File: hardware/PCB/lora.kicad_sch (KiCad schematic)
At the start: 8 parts, among them J2 LoRa_prog, U7 WLR089U0-I_RM

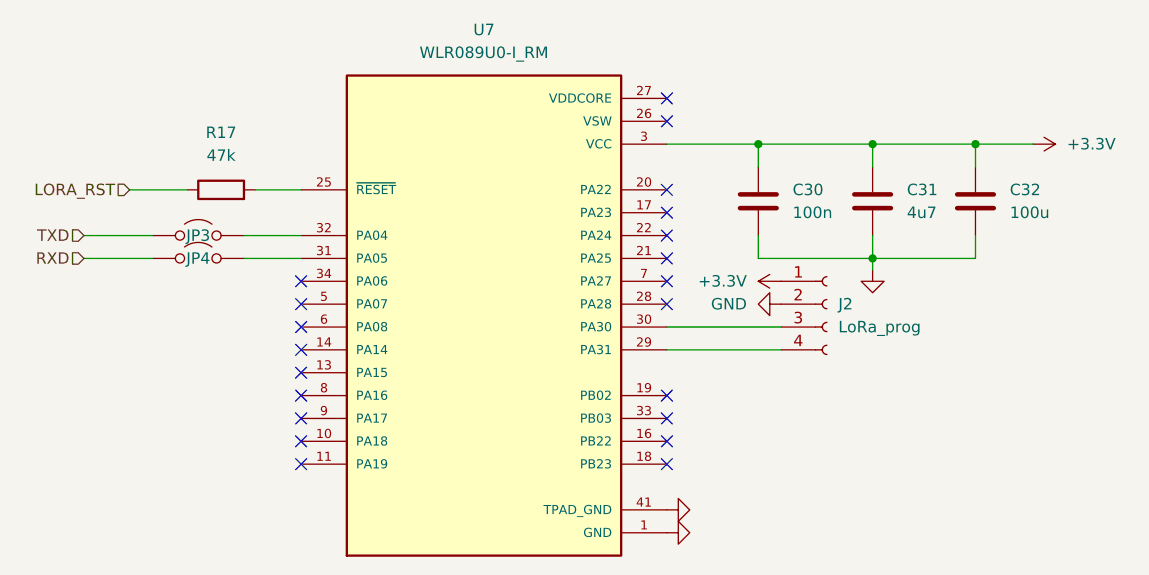
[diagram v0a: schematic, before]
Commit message: Changed LoRa modul on PCB
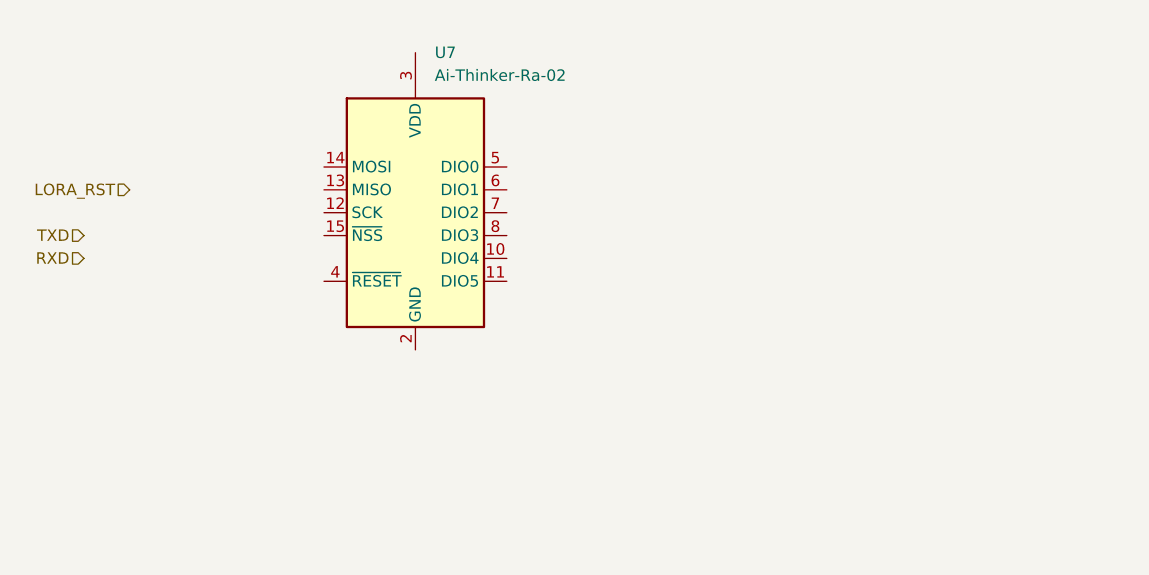
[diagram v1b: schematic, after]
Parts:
- removed C30: 100n, Capacitor_SMD:C_1206_3216Metric_Pad1.33x1.80mm_HandSolder, symbol Device:C
- removed C31: 4u7, Capacitor_SMD:C_1206_3216Metric_Pad1.33x1.80mm_HandSolder, symbol Device:C
- removed C32: 100u, Capacitor_SMD:C_1206_3216Metric_Pad1.33x1.80mm_HandSolder, symbol Device:C
- removed J2: LoRa_prog, Connector_PinSocket_2.54mm:PinSocket_1x04_P2.54mm_Vertical, symbol Connector:Conn_01x04_Socket
- removed JP3, JP4: Jumper_2_Open, Jumper:SolderJumper-2_P1.3mm_Open_RoundedPad1.0x1.5mm, symbol Jumper:Jumper_2_Open
- removed R17: 47k, Resistor_SMD:R_1206_3216Metric_Pad1.30x1.75mm_HandSolder, symbol Device:R
- removed U7: WLR089U0-I_RM, WLR089U0-I_RM:MODULE_WLR089U0-I_RM, symbol WLR089U0-I_RM:WLR089U0-I_RM
- added U7: Ai-Thinker-Ra-02, RF_Module:Ai-Thinker-Ra-01-LoRa, symbol RF_Module:Ai-Thinker-Ra-02
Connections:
- new net: U7.1 (GND), U7.16 (GND), U7.2 (GND), U7.9 (GND)
- no-connect marks 21 -> 0

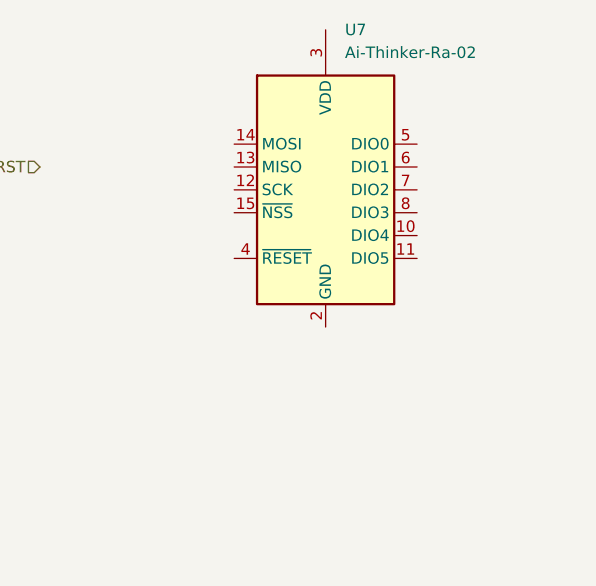
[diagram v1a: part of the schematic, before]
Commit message: Added I2C expander for motor drivers and changed LoRa module
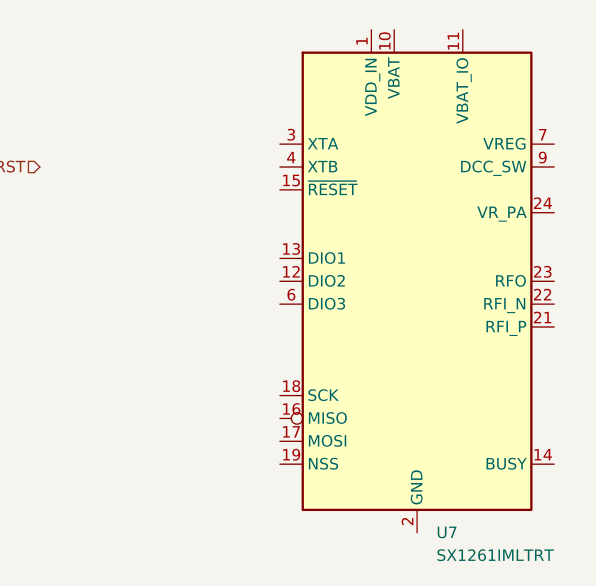
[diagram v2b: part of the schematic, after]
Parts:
- removed U7: Ai-Thinker-Ra-02, RF_Module:Ai-Thinker-Ra-01-LoRa, symbol RF_Module:Ai-Thinker-Ra-02
- added U7: SX1261IMLTRT, Package_DFN_QFN:QFN-24-1EP_4x4mm_P0.5mm_EP2.15x2.15mm, symbol RF:SX1261IMLTRT
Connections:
- new net: U7.2 (GND), U7.20 (GND), U7.25 (GND), U7.5 (GND), U7.8 (GND)
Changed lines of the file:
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@@
 	)
 	(symbol
-		(lib_id "RF_Module:Ai-Thinker-Ra-02")
-		(at 127 69.85 0)
+		(lib_id "RF:SX1261IMLTRT")
+		(at 137.16 80.01 0)
 		(unit 1)
 		(exclude_from_sim no)
@@
 		(fields_autoplaced yes)
 		(property "Reference" "U7"
-			(at 129.1433 52.07 0)
+			(at 139.3033 107.95 0)
 			(effects
 				(font
@@
 			)
 		)
-		(property "Value" "Ai-Thinker-Ra-02"
-			(at 129.1433 54.61 0)
+		(property "Value" "SX1261IMLTRT"
+			(at 139.3033 110.49 0)
 			(effects
 				(font
@@
 			)
 		)
-		(property "Footprint" "RF_Module:Ai-Thinker-Ra-01-LoRa"
-			(at 152.4 80.01 0)
+		(property "Footprint" "Package_DFN_QFN:QFN-24-1EP_4x4mm_P0.5mm_EP2.15x2.15mm"
+			(at 138.43 111.76 0)
 			(effects
 				(font
@@
 			)
 		)
-		(property "Datasheet" "http://wiki.ai-thinker.com/_media/lora/docs/c048ps01a1_ra-02_product_specification_v1.1.pdf"
-			(at 129.54 50.8 0)
+		(property "Datasheet" "https://semtech.file.force.com/sfc/dist/version/download/?oid=00DE0000000JelG&ids=0682R00000IjPWSQA3&d=%2Fa%2F2R000000Un7F%2FyT.fKdAr9ZAo3cJLc4F2cBdUsMftpT2vsOICP7NmvMo"
+			(at 138.43 109.22 0)
 			(effects
 				(font
@@
 			)
 		)
-		(property "Description" "Ai-Thinker Ra-02 410-525 MHz LoRa Module, SPI interface, U.FL antenna connector"
-			(at 127 69.85 0)
+		(property "Description" "150 MHz to 960 MHz Low Power Long Range Transceiver, 14dBm output power, spreading factor from 5 to 12, LoRA, QFN-24"
+			(at 137.16 80.01 0)
 			(effects
 				(font
@@
 			)
 		)
-		(pin "11"
+		(pin "20"
+		)
+		(pin "2"
+		)
+		(pin "14"
 		)
 		(pin "10"
 		)
-		(pin "14"
+		(pin "9"
+		)
+		(pin "18"
+		)
+		(pin "21"
+		)
+		(pin "24"
+		)
+		(pin "6"
 		)
 		(pin "13"
 		)
-		(pin "12"
-		)
 		(pin "15"
-		)
-		(pin "2"
 		)
 		(pin "4"
@@
 		(pin "3"
 		)
-		(pin "1"
+		(pin "8"
+		)
+		(pin "25"
+		)
+		(pin "11"
+		)
+		(pin "22"
+		)
+		(pin "23"
+		)
+		(pin "19"
+		)
+		(pin "5"
 		)
 		(pin "7"
 		)
-		(pin "8"
+		(pin "1"
 		)
-		(pin "6"
-		)
-		(pin "5"
-		)
-		(pin "9"
+		(pin "12"
 		)
 		(pin "16"
 		)
+		(pin "17"
+		)
 		(instances

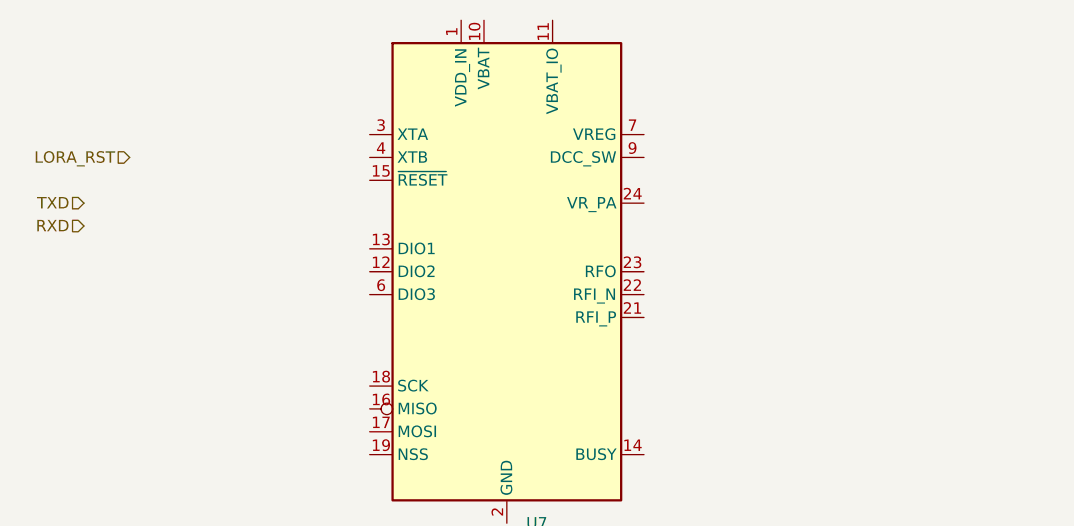
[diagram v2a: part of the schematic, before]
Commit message: Started RF design for LoRa chip
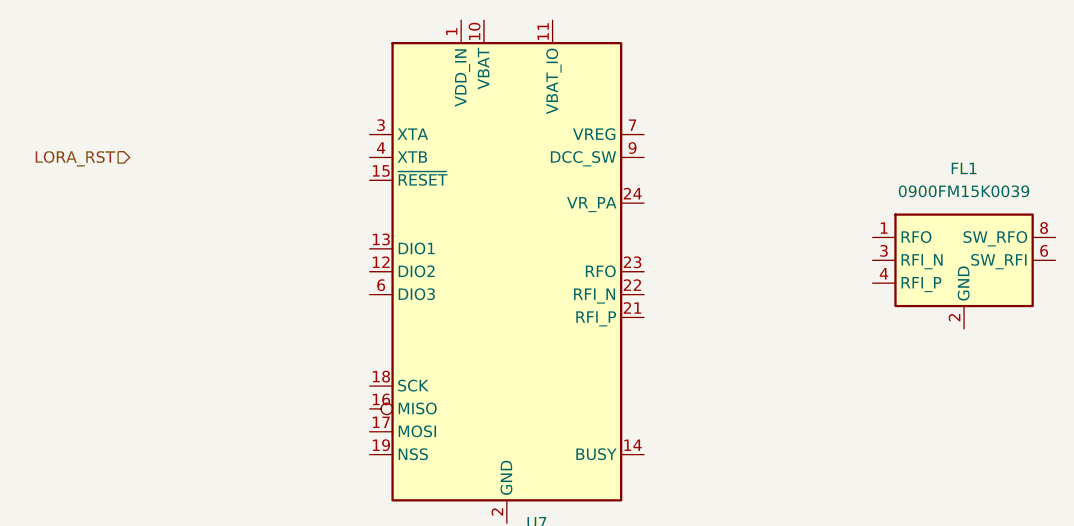
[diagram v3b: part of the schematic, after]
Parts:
- added FL1: 0900FM15K0039, RF_Converter:Balun_Johanson_0900FM15K0039, symbol Filter:0900FM15K0039
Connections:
- new net: FL1.10 (GND), FL1.2 (GND), FL1.5 (GND), FL1.7 (GND), FL1.9 (GND)
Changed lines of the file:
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@@
-		)
-	)
-	(hierarchical_label "TXD"
-		(shape input)
-		(at 90.17 72.39 180)
-		(effects
-			(font
-				(size 1.27 1.27)
-			)
-			(justify right)
-		)
-	)
-	(hierarchical_label "RXD"
-		(shape input)
-		(at 90.17 74.93 180)
-		(effects
-			(font
-				(size 1.27 1.27)
-			)
-			(justify right)
 		)
 	)
@@
 					(unit 1)
 				)
+			)
+		)
+	)
+	(symbol
+		(lib_id "Filter:0900FM15K0039")
+		(at 187.96 78.74 0)
+		(unit 1)
+		(exclude_from_sim no)
+		(in_bom yes)
+		(on_board yes)
+		(dnp no)
+		(fields_autoplaced yes)
+		(property "Reference" "FL1"
+			(at 187.96 68.58 0)
+			(effects
+				(font
+					(size 1.27 1.27)
+				)
+			)
+		)
+		(property "Value" "0900FM15K0039"
+			(at 187.96 71.12 0)
+			(effects
+				(font
+					(size 1.27 1.27)
+				)
+			)
+		)
+		(property "Footprint" "RF_Converter:Balun_Johanson_0900FM15K0039"
+			(at 187.96 88.265 0)
+			(effects
+				(font
+					(size 1.27 1.27)
+				)
+				(hide yes)
+			)
+		)
+		(property "Datasheet" "https://www.johansontechnology.com/datasheets/0900FM15K0039/0900FM15K0039.pdf"
+			(at 188.595 90.17 0)
+			(effects
+				(font
+					(size 1.27 1.27)
+				)
+				(hide yes)
+			)
+		)
+		(property "Description" "868MHz/915MHz Sub-GHz Impedance Matched Filter integrated passive for Semtech SX1261, SX1262, LLCC68"
+			(at 187.96 78.74 0)
+			(effects
+				(font
+					(size 1.27 1.27)
+				)
+				(hide yes)
+			)
+		)
+		(pin "6"
+		)
+		(pin "10"
+		)
+		(pin "9"
+		)
+		(pin "1"
+		)
+		(pin "8"
+		)
+		(pin "2"
+		)
+		(pin "4"
+		)
+		(pin "3"
+		)
+		(pin "7"
+		)
+		(pin "5"
+		)
+		(instances
+			(project ""
+				(path "/45ea479c-a8ef-4c14-88b0-391ede4fd156/efc52d26-5e7f-40f5-a09a-58b8b5321559"
+					(reference "FL1")
+					(unit 1)
+				)

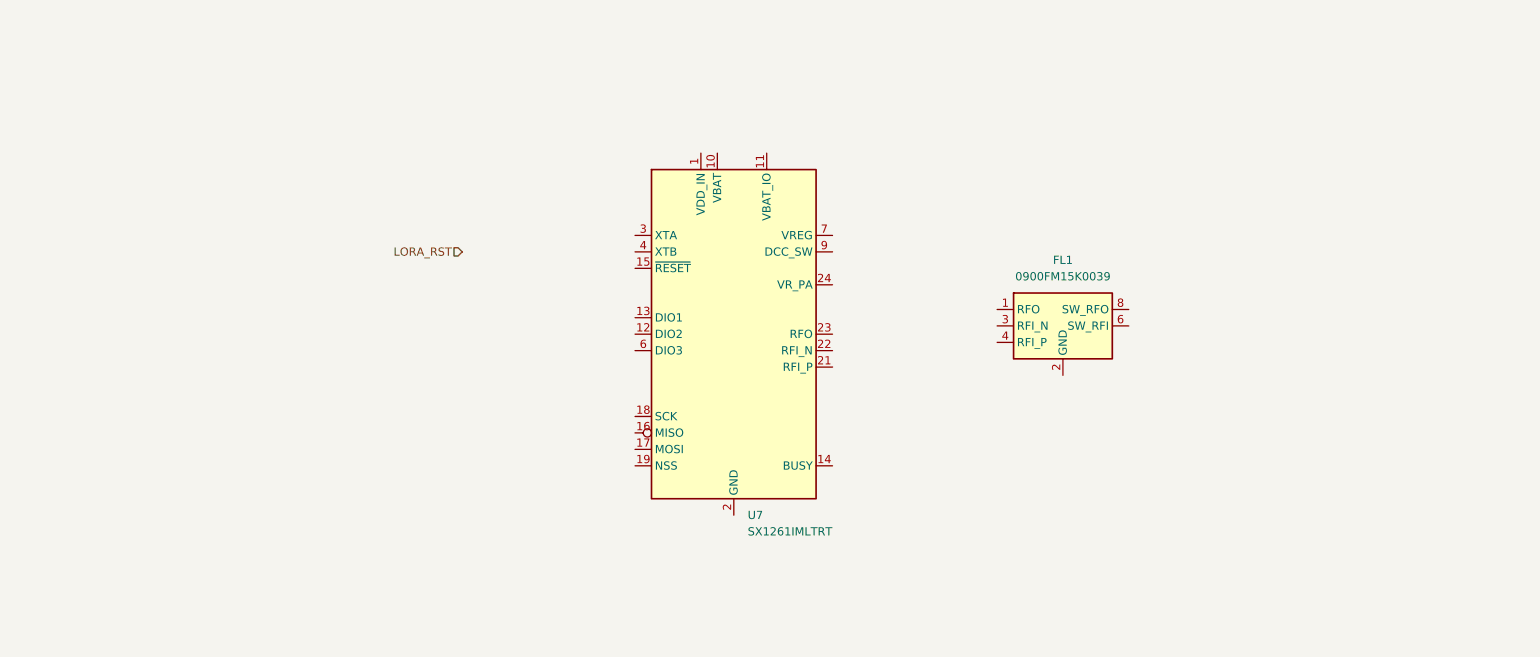
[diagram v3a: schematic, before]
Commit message: Started shcematic design for LoRa chip
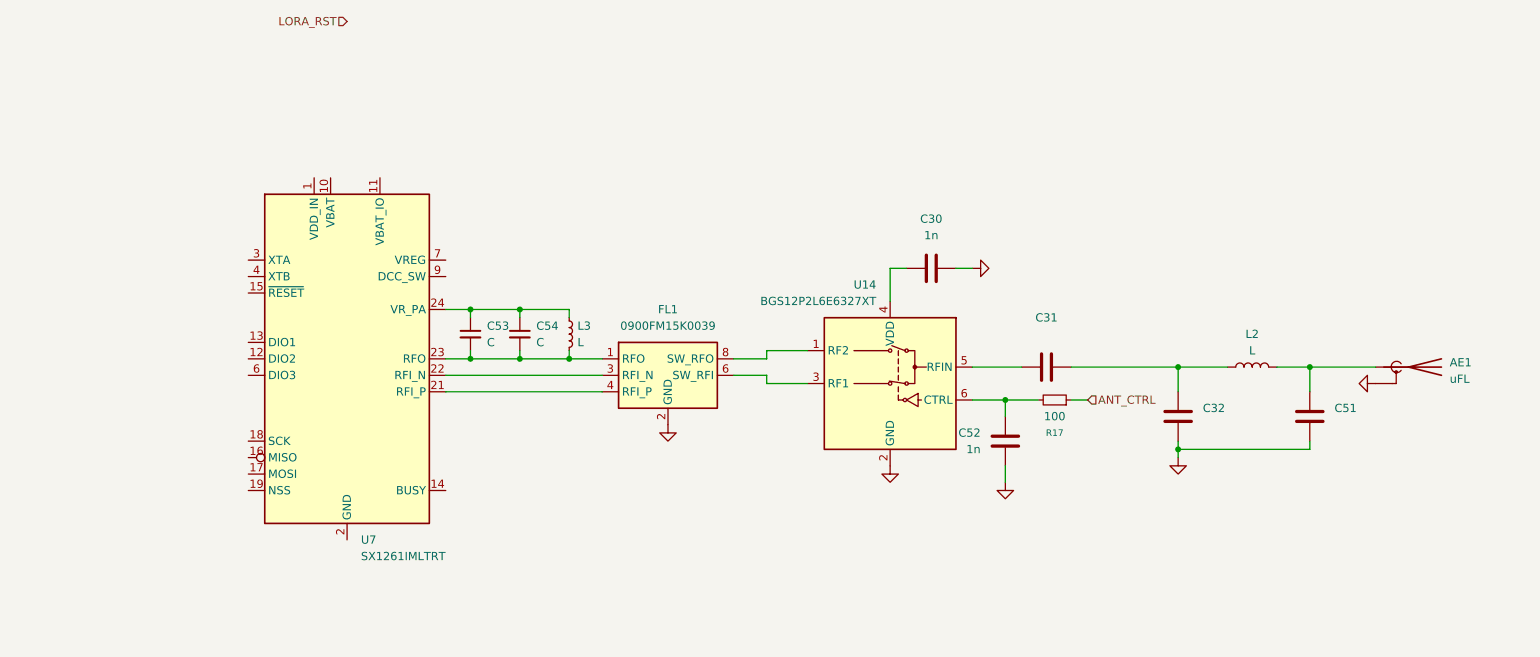
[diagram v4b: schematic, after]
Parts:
- added AE1: uFL, symbol Device:Antenna_Shield
- added C30, C52: 1n, symbol Device:C
- added C31, C32, C51: ~, symbol Device:C
- added C53, C54: C, symbol Device:C_Small
- added L2: L, symbol Device:L
- added L3: L, symbol Device:L_Small
- added R17: 100, symbol Device:R_Small
- added U14: BGS12P2L6E6327XT, Package_LGA:Infineon_PG-TSNP-6-10_0.7x1.1mm_0.7x1.1mm_P0.4mm, symbol RF_Switch:BGS12WN6E6327
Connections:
- net at U7.21 (RFI_P): now also FL1.4 (RFI_P)
- net at U7.22 (RFI_N): now also FL1.3 (RFI_N)
- net at U7.23 (RFO): now also FL1.1 (RFO), C53.2, C54.2, L3.2
- net at U7.24 (VR_PA): now also C53.1, C54.1, L3.1
- net GND: now reaches FL1.10 (GND), FL1.2 (GND), FL1.5 (GND), FL1.7 (GND), FL1.9 (GND)
- net GND: now also AE1.2 (Shield), C30.2, C32.1, C51.1, C52.1, U14.2 (GND)
- net at FL1.6 (SW_RFI): now also U14.3 (RF1)
- net at FL1.8 (SW_RFO): now also U14.1 (RF2)
- new net: C30.1, U14.4 (VDD)
- new net: C52.2, R17.2, U14.6 (CTRL)
- new net: C31.2, C32.2, L2.1
- new net: C31.1, U14.5 (RFIN)
- new net: AE1.1 (A), C51.2, L2.2
- new net ANT_CTRL: R17.1
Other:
- moved on the sheet: FL1, U7

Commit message: Finished schematic for LoRa, added BME280
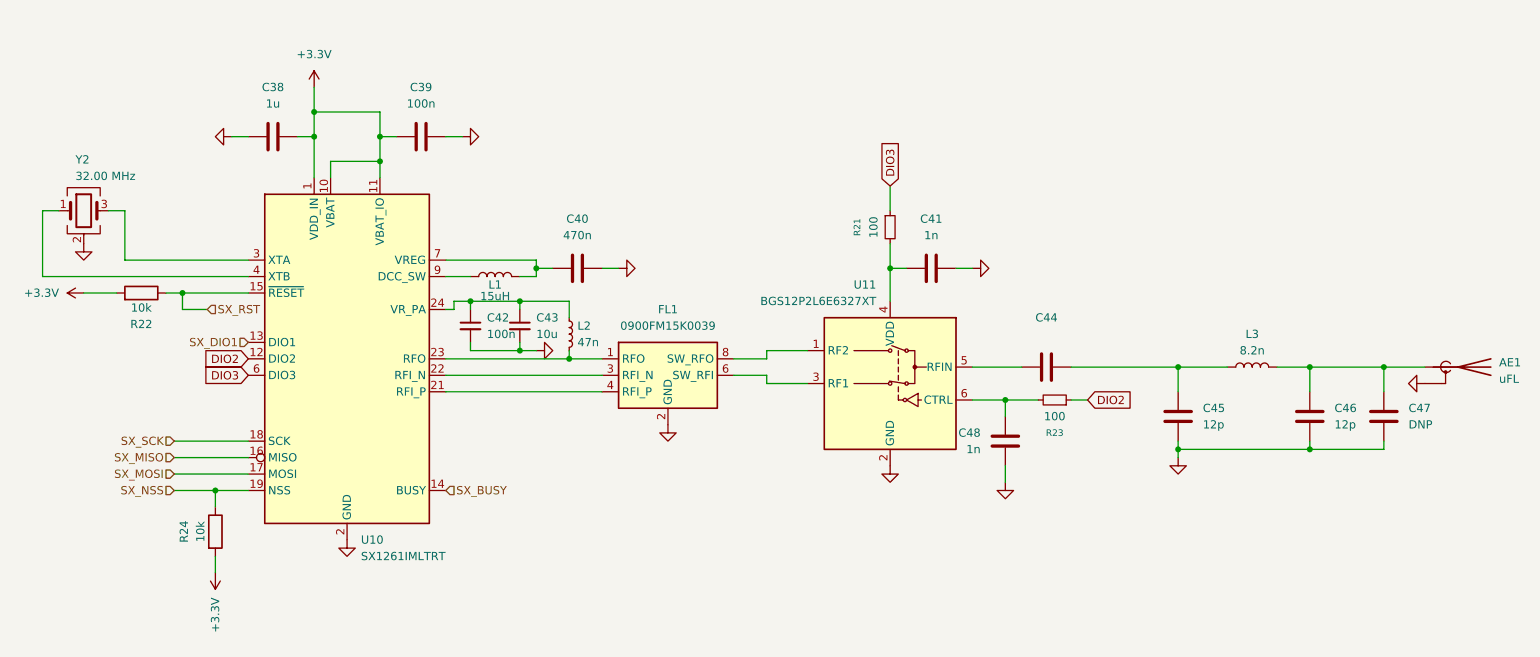
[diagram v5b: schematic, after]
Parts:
- added C38: 1u, symbol Device:C
- added C39: 100n, symbol Device:C
- added C40: 470n, symbol Device:C
- added C47: DNP, symbol Device:C
- added L1: 15uH, symbol Device:L
- added R21: 100, symbol Device:R_Small
- added R22, R24: 10k, symbol Device:R
- added Y2: 32.00 MHz, saját:Crystal_SMD_Abracon_ABM10N-4Pin_2.5x2.0mm, symbol Device:Crystal_GND24
- C42: renamed from C53; value C -> 100n
- C43: renamed from C54; value C -> 10u
- C45: renamed from C32; value ~ -> 12p
- C46: renamed from C51; value ~ -> 12p
- L2: renamed from L3; value L -> 47n
- L3: renamed from L2; value L -> 8.2n
- renumbered C30 to C41, C31 to C44, C52 to C48, R17 to R23, U7 to U10, U14 to U11
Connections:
- net ANT_CTRL is gone; now on net DIO2: R23.1
- net GND: now also C42.2, C43.2, U10.2 (GND), U10.20 (GND), U10.25 (GND), U10.5 (GND), U10.8 (GND), C38.2, C39.2, C40.2, C47.1, Y2.2 (G), Y2.4 (G)
- net at C41.1, U11.4 (VDD): now also R21.2
- net +3.3V: now reaches U10.1 (VDD_IN)
- net +3.3V: now also U10.10 (VBAT), U10.11 (VBAT_IO), C38.1, C39.1, R22.2, R24.2
- net DIO2: now reaches U10.12 (DIO2)
- net SX_DIO1: now reaches U10.13 (DIO1)
- net SX_BUSY: now reaches U10.14 (BUSY)
- net SX_RST: now reaches U10.15 (~{RESET})
- net SX_RST: now also R22.1
- net SX_MISO: now reaches U10.16 (MISO)
- net SX_MOSI: now reaches U10.17 (MOSI)
- net SX_SCK: now reaches U10.18 (SCK)
- net SX_NSS: now reaches U10.19 (NSS)
- net SX_NSS: now also R24.1
- net at FL1.1 (RFO), L2.2, U10.23 (RFO): no longer C42.2, C43.2
- net at U10.3 (XTA): now also Y2.3
- net at U10.4 (XTB): now also Y2.1
- net DIO3: now reaches U10.6 (DIO3)
- net DIO3: now also R21.1
- net at U10.7 (VREG): now also C40.1, L1.2
- net at U10.9 (DCC_SW): now also L1.1
- net at AE1.1 (A), C46.2, L3.2: now also C47.2
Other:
- moved on the sheet: AE1, C42, C43
